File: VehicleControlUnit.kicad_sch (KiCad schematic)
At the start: 33 parts, among them J1 Conn_01x02, J10 CAR_CAN_Breakout, J2 Precharge_Ready, J4 Conn_01x02, J5 Conn_01x02, J6 Conn_01x08, J7 Conn_01x04, J8 Conn_01x04, J9 MOTOR_CAN_Breakout, Q1 PMV35EPER

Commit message: fuck the rats nest im doing it tomorrow
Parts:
- removed J10: CAR_CAN_Breakout, Connector_PinHeader_2.54mm:PinHeader_1x02_P2.54mm_Vertical, symbol Connector_Generic:Conn_01x02
- removed J2: Precharge_Ready, Connector_Molex:Molex_Nano-Fit_105309-xx02_1x02_P2.50mm_Vertical, symbol Connector_Generic:Conn_01x02
- removed J6: Conn_01x08, Connector_PinHeader_2.54mm:PinHeader_1x08_P2.54mm_Vertical, symbol Connector_Generic:Conn_01x08
- removed J9: MOTOR_CAN_Breakout, Connector_PinHeader_2.54mm:PinHeader_1x02_P2.54mm_Vertical, symbol Connector_Generic:Conn_01x02
- removed Q1: PMV35EPER, Package_TO_SOT_SMD:SOT-23-3, symbol Device:Q_PMOS
- removed R1: 49.9k, Resistor_SMD:R_0805_2012Metric, symbol Device:R_US
- removed R2: 100, Resistor_SMD:R_0805_2012Metric, symbol Device:R_US
- removed R3: 10k, Resistor_SMD:R_0805_2012Metric, symbol Device:R_US
- added C2: 22n, Capacitor_SMD:C_0805_2012Metric, symbol Device:C
- added J5, J6: SFH11-PBPC-D05-ST-BK, UTSVT_Connectors:CONN_SFH11-xxxC-D05-ST-XX_SUL, symbol UTSVT_Connectors:SFH11-PBPC-D05-ST-BK
- added Q1: PSMN8R5-40MSDX, UTSVT_Power:BUK7M1780EX, symbol UTSVT_Power:PSMN8R5-40MSDX
- added U1: LM74501-Q1, Package_TO_SOT_SMD:SOT-23-8, symbol UTSVT_ICs:LM74501-Q1
- C1: value 1u -> 220n
- D1: footprint Active-PrechargeLib:BZT52B12QX -> UTSVT_Passives:BZT52B12QX
- J1: footprint utsvt_conn:Molex_MicroFit3.0_1x2xP3.00mm_PolarizingPeg_Vertical -> UTSVT_Connectors:Molex_MicroFit3.0_1x2xP3.00mm_PolarizingPeg_Vertical
- J4: renamed from J3; footprint (none) -> UTSVT_Special:LeaderSOM
- renumbered C2 to C3, C3 to C4, J4 to J2, J5 to J3, R4 to R1, R5 to R2, R6 to R3, R7 to R4, R8 to R5
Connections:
- net +24V: now also Q1.10 (D_6), Q1.11 (D_7), Q1.5 (D_1), Q1.6 (D_2), Q1.7 (D_3), Q1.8 (D_4), Q1.9 (D_5), U1.8 (Drain)
- net C_CAN_H: now also J6.3
- net C_CAN_L: now also J6.4
- net ESP_RX: now also J6.5
- net ESP_TX: now also J6.6
- net GND: now also D1.2 (A), J5.10, J6.10, U1.5 (GND); no longer C1.2
- net LV+: now also C1.2, C2.2, Q1.1 (S_1), Q1.2 (S_2), Q1.3 (S_3), U1.2 (Source), U1.6 (EN)
- net MPre_Enable: now also J5.2
- net MPre_Sense: now also J5.4
- net M_CAN_H: now also J6.1
- net M_CAN_L: now also J6.2
- net M_Enable: now also J5.1
- net M_Sense: now also J5.3
- net Precharge_Ready: now also J5.8; no longer C1.1
- net VPrecharge+: now also J5.6
- net VPrecharge-: now also J5.7
- new net: C1.1, U1.3 (VCap)
- new net: C2.1, Q1.4 (G), U1.1 (Gate)
- no-connect marks 5 -> 12
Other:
- note added: "Precharge Board Connectors"
- note removed: "From Optocoupler on Precharge Board"
- note removed: "Lowpass Filter Fc = 1.6kHz"
- note removed: "Precharge Connectors"
- moved on the sheet: 24V_TP1, D1, J1, J2, J3, J7, J8, LVGND_TP1

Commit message: routing done
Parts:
- added C19: 0.1u, Capacitor_SMD:C_0805_2012Metric, symbol Device:C
- J2, J3: footprint Connector_Molex:Molex_Nano-Fit_105309-xx02_1x02_P2.50mm_Vertical -> UTSVT_Connectors:Molex_Nano-Fit_105309-xx02_1x02_P2.50mm_Vertical
- J7, J8: footprint Connector_Molex:Molex_Nano-Fit_105309-xx04_1x04_P2.50mm_Vertical -> UTSVT_Connectors:Molex_Nano-Fit_105309-xx04_1x04_P2.50mm_Vertical
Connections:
- net Precharge_Ready is gone; now on net MPre_Sense: J5.8
- net 3V3_LSOM: now also J5.1
- net ESP_RX: now also J6.6; no longer J6.5
- net ESP_TX: now also J6.5; no longer J6.6
- net GND: now also J5.9, J6.9, C19.2
- net LV+: now also C19.1
- net MPre_Enable: now also J5.3; no longer J5.2
- net MPre_Sense: no longer J5.4
- net M_Enable: now also J5.2; no longer J5.1
- net M_Sense: now also J5.7; no longer J5.3
- net VPrecharge-: now also J5.4; no longer J5.7
- no-connect marks 12 -> 10
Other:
- moved on the sheet: C3, C4, LVPWR1, R1

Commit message: replace microfit with nanofit and some layout adjustments
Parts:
- J1: footprint UTSVT_Connectors:Molex_MicroFit3.0_1x2xP3.00mm_PolarizingPeg_Vertical -> UTSVT_Connectors:Molex_Nano-Fit_105309-xx02_1x02_P2.50mm_Vertical
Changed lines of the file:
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@@
 			)
 		)
-		(property "Footprint" "UTSVT_Connectors:Molex_MicroFit3.0_1x2xP3.00mm_PolarizingPeg_Vertical"
+		(property "Footprint" "UTSVT_Connectors:Molex_Nano-Fit_105309-xx02_1x02_P2.50mm_Vertical"
 			(at 26.035 41.91 0)
 			(effects

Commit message: lakshay nitpicks
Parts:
- removed J6: SFH11-PBPC-D05-ST-BK, UTSVT_Connectors:CONN_SFH11-xxxC-D05-ST-XX_SUL, symbol UTSVT_Connectors:SFH11-PBPC-D05-ST-BK
- added J8: Conn_01x04, Connector_PinHeader_2.54mm:PinHeader_1x04_P2.54mm_Vertical, symbol Connector_Generic:Conn_01x04
- renumbered C19 to C5, J7 to J6, J8 to J7
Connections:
- net 3V3_LSOM: no longer J5.1
- net C_CAN_H: now also J6.4 (Pin_4), J8.4 (Pin_4); no longer J6.2 (Pin_2)
- net C_CAN_L: now also J6.3 (Pin_3), J8.3 (Pin_3); no longer J6.1 (Pin_1)
- net ESP_RX: now also J5.8
- net ESP_TX: now also J5.7
- net MPre_Enable: now also J5.2; no longer J5.3
- net MPre_Sense: now also J5.3; no longer J5.8
- net M_CAN_H: now also J6.2 (Pin_2), J8.2 (Pin_2); no longer J6.4 (Pin_4)
- net M_CAN_L: now also J6.1 (Pin_1), J8.1 (Pin_1); no longer J6.3 (Pin_3)
- net M_Enable: now also J5.4; no longer J5.2
- net M_Sense: now also J5.1; no longer J5.7
- net Motor_Voltage: now reaches J5.5
- net Motor_Voltage: now also J3.2 (Pin_2), J4.16 (SPI2_CS)
- net VPrecharge+ renamed Batt_Voltage
- removed net VPrecharge-: J3.2 (Pin_2), J4.16 (SPI2_CS), J5.4
- no-connect marks 10 -> 7

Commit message: cubemx stuff
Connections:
- net ESP_RX: now also J4.19 (UART5_RX), J5.7; no longer J4.17 (UART5_TX), J5.8
- net ESP_TX: now also J4.17 (UART5_TX), J5.8; no longer J4.19 (UART5_RX), J5.7
- net MPre_Enable: now also J4.16 (SPI2_CS); no longer J4.9 (I2C3_SDA)
- net Motor_Voltage: now also J4.9 (I2C3_SDA); no longer J4.16 (SPI2_CS)
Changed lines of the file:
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@@
+	(wire
+		(pts
+			(xy 44.45 109.22) (xy 31.75 109.22)
+		)
+		(stroke
+			(width 0)
+			(type default)
+		)
+	)
 	(wire
 		(pts
@@
 	(wire
 		(pts
-			(xy 77.47 101.6) (xy 95.25 101.6)
-		)
-		(stroke
-			(width 0)
-			(type default)
-		)
-	)
-	(wire
-		(pts
 			(xy 199.39 27.94) (xy 199.39 30.48)
 		)
@@
 	(wire
 		(pts
+			(xy 95.25 101.6) (xy 77.47 101.6)
+		)
+		(stroke
+			(width 0)
+			(type default)
+		)
+	)
+	(wire
+		(pts
 			(xy 76.835 32.385) (xy 76.835 34.925)
 		)
@@
 		(pts
 			(xy 243.84 125.73) (xy 248.92 125.73)
-		)
-		(stroke
-			(width 0)
-			(type default)
-		)
-	)
-	(wire
-		(pts
-			(xy 31.75 109.22) (xy 44.45 109.22)
 		)
 		(stroke
@@
 		)
 	)
-	(label "MPre_Enable"
-		(at 31.75 109.22 0)
-		(effects
-			(font
-				(size 1.27 1.27)
-			)
-			(justify left bottom)
-		)
-	)
 	(label "M_CAN_L"
 		(at 236.22 58.42 0)
@@
 		)
 	)
+	(label "ESP_RX"
+		(at 166.37 113.03 0)
+		(effects
+			(font
+				(size 1.27 1.27)
+			)
+			(justify left bottom)
+		)
+	)
 	(label "M_Sense"
 		(at 166.37 97.79 0)
@@
 	)
 	(label "ESP_RX"
-		(at 35.56 99.06 0)
+		(at 35.56 96.52 0)
 		(effects
 			(font
@@
 		)
 	)
+	(label "Motor_Voltage"
+		(at 31.75 109.22 0)
+		(effects
+			(font
+				(size 1.27 1.27)
+			)
+			(justify left bottom)
+		)
+	)
 	(label "LED1"
 		(at 165.1 27.94 0)
@@
 		)
 	)
+	(label "ESP_TX"
+		(at 166.37 115.57 0)
+		(effects
+			(font
+				(size 1.27 1.27)
+			)
+			(justify left bottom)
+		)
+	)
 	(label "C_CAN_L"
 		(at 236.22 33.655 0)
@@
 		)
 	)
-	(label "ESP_TX"
-		(at 35.56 96.52 0)
-		(effects
-			(font
-				(size 1.27 1.27)
-			)
-			(justify left bottom)
-		)
-	)
 	(label "C_CAN_H"
 		(at 236.22 36.195 0)
@@
 		)
 	)
-	(label "ESP_RX"
-		(at 166.37 115.57 0)
-		(effects
-			(font
-				(size 1.27 1.27)
-			)
-			(justify left bottom)
-		)
-	)
 	(label "LED4"
 		(at 199.39 27.94 0)
@@
 		)
 	)
-	(label "ESP_TX"
-		(at 166.37 113.03 0)
-		(effects
-			(font
-				(size 1.27 1.27)
-			)
-			(justify left bottom)
-		)
-	)
 	(label "C_CAN_L"
 		(at 162.56 111.76 180)
@@
 		)
 	)
+	(label "MPre_Enable"
+		(at 95.25 101.6 180)
+		(effects
+			(font
+				(size 1.27 1.27)
+			)
+			(justify right bottom)
+		)
+	)
 	(label "C_CAN_L"
 		(at 236.22 48.26 0)
@@
 		)
 	)
+	(label "ESP_TX"
+		(at 35.56 99.06 0)
+		(effects
+			(font
+				(size 1.27 1.27)
+			)
+			(justify left bottom)
+		)
+	)
 	(label "M_CAN_H"
 		(at 236.22 45.72 0)
@@
 		(effects
 			(font
-				(size 1.27 1.27)
-			)
-			(justify right bottom)
-		)
-	)
-	(label "Motor_Voltage"
-		(at 95.25 101.6 180)
-		(effects
-			(font

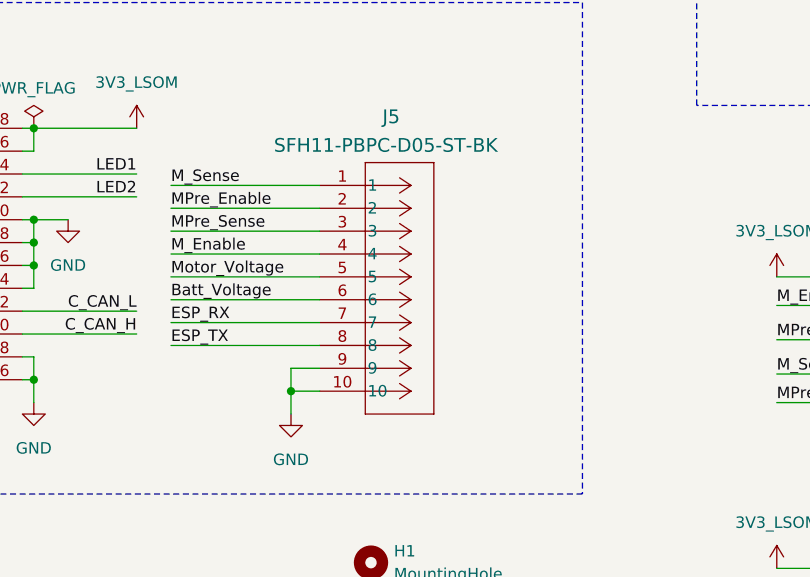
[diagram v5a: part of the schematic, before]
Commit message: replaced 0805 with 0603, changed logic analyzer symbol and silkscreen
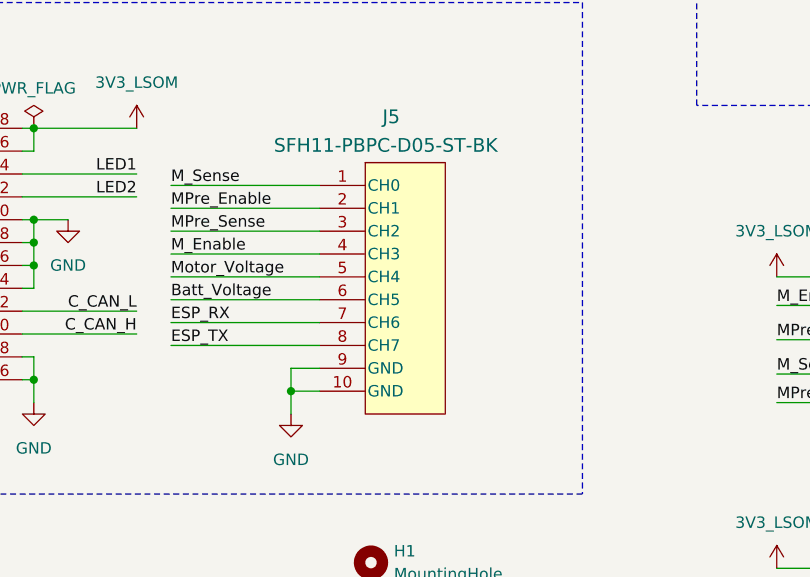
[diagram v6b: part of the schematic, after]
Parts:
- C1, C2, C3, C4, C5: footprint Capacitor_SMD:C_0805_2012Metric -> Capacitor_SMD:C_0603_1608Metric
- LED1, LED2, LED3, LED4, LVPWR1: footprint LED_SMD:LED_0805_2012Metric -> LED_SMD:LED_0603_1608Metric
- R1, R2, R3, R4, R5: footprint Resistor_SMD:R_0805_2012Metric -> Resistor_SMD:R_0603_1608Metric
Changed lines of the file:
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@@
 			)
 		)
-		(property "Footprint" "Capacitor_SMD:C_0805_2012Metric"
+		(property "Footprint" "Capacitor_SMD:C_0603_1608Metric"
 			(at 46.0502 52.705 0)
 			(effects
@@
 			)
 		)
-		(property "Footprint" "LED_SMD:LED_0805_2012Metric"
+		(property "Footprint" "LED_SMD:LED_0603_1608Metric"
 			(at 187.96 43.18 0)
 			(effects
@@
 			)
 		)
-		(property "Footprint" "Resistor_SMD:R_0805_2012Metric"
+		(property "Footprint" "Resistor_SMD:R_0603_1608Metric"
 			(at 166.116 34.544 90)
 			(effects
@@
 			)
 		)
-		(property "Footprint" "Capacitor_SMD:C_0805_2012Metric"
+		(property "Footprint" "Capacitor_SMD:C_0603_1608Metric"
 			(at 141.3002 41.91 0)
 			(effects
@@
 			)
 		)
-		(property "Footprint" "Resistor_SMD:R_0805_2012Metric"
+		(property "Footprint" "Resistor_SMD:R_0603_1608Metric"
 			(at 188.976 34.544 90)
 			(effects
@@
 			)
 		)
-		(property "Footprint" "LED_SMD:LED_0805_2012Metric"
+		(property "Footprint" "LED_SMD:LED_0603_1608Metric"
 			(at 199.39 43.18 0)
 			(effects
@@
 			)
 		)
-		(property "Footprint" "Capacitor_SMD:C_0805_2012Metric"
+		(property "Footprint" "Capacitor_SMD:C_0603_1608Metric"
 			(at 49.8602 34.29 0)
 			(effects
@@
 			)
 		)
-		(property "Footprint" "Resistor_SMD:R_0805_2012Metric"
+		(property "Footprint" "Resistor_SMD:R_0603_1608Metric"
 			(at 200.406 34.544 90)
 			(effects
@@
 			)
 		)
-		(property "Footprint" "Resistor_SMD:R_0805_2012Metric"
+		(property "Footprint" "Resistor_SMD:R_0603_1608Metric"
 			(at 177.546 34.544 90)
 			(effects
@@
 			)
 		)
-		(property "Footprint" "Capacitor_SMD:C_0805_2012Metric"
+		(property "Footprint" "Capacitor_SMD:C_0603_1608Metric"
 			(at 131.1402 41.91 0)
 			(effects
@@
 			)
 		)
-		(property "Footprint" "Resistor_SMD:R_0805_2012Metric"
+		(property "Footprint" "Resistor_SMD:R_0603_1608Metric"
 			(at 105.156 33.274 90)
 			(effects
@@
 			)
 		)
-		(property "Footprint" "LED_SMD:LED_0805_2012Metric"
+		(property "Footprint" "LED_SMD:LED_0603_1608Metric"
 			(at 165.1 43.18 0)
 			(effects
@@
 			)
 		)
-		(property "Footprint" "Capacitor_SMD:C_0805_2012Metric"
+		(property "Footprint" "Capacitor_SMD:C_0603_1608Metric"
 			(at 118.4402 41.91 0)
 			(effects
@@
 			)
 		)
-		(property "Footprint" "LED_SMD:LED_0805_2012Metric"
+		(property "Footprint" "LED_SMD:LED_0603_1608Metric"
 			(at 176.53 43.18 0)
 			(effects
@@
 			)
 		)
-		(property "Footprint" "LED_SMD:LED_0805_2012Metric"
+		(property "Footprint" "LED_SMD:LED_0603_1608Metric"
 			(at 104.14 41.91 0)
 			(effects

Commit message: embedding 3d models
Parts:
- U1: footprint Package_TO_SOT_SMD:SOT-23-8 -> UTSVT_ICs:LM74501QDDFRQ1
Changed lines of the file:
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@@
 			)
 		)
-		(property "Footprint" "Package_TO_SOT_SMD:SOT-23-8"
+		(property "Footprint" "UTSVT_ICs:LM74501QDDFRQ1"
 			(at 64.135 48.26 0)
 			(effects

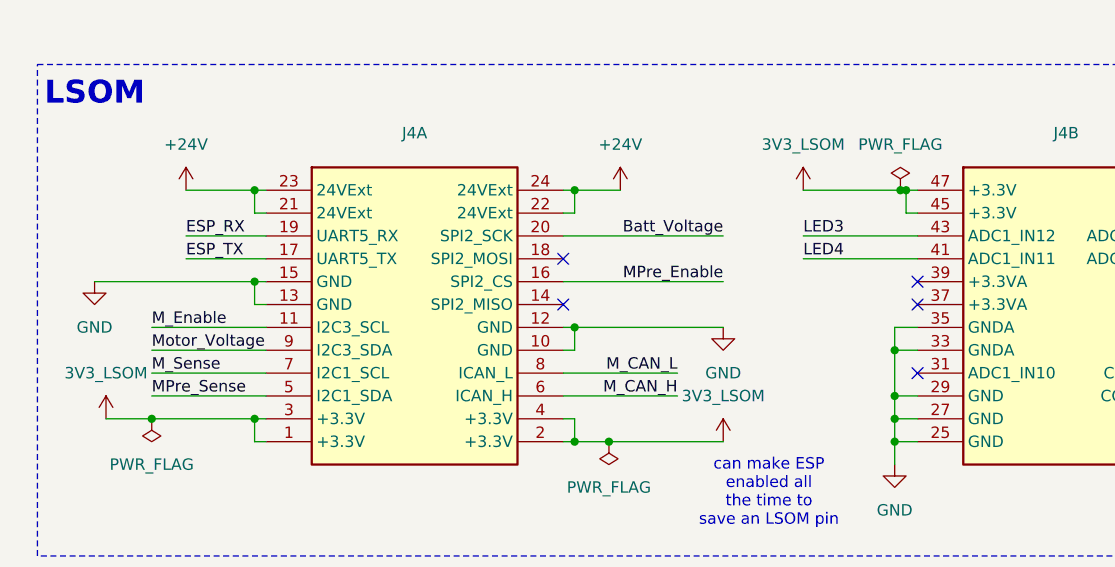
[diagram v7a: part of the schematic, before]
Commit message: added image to schematic
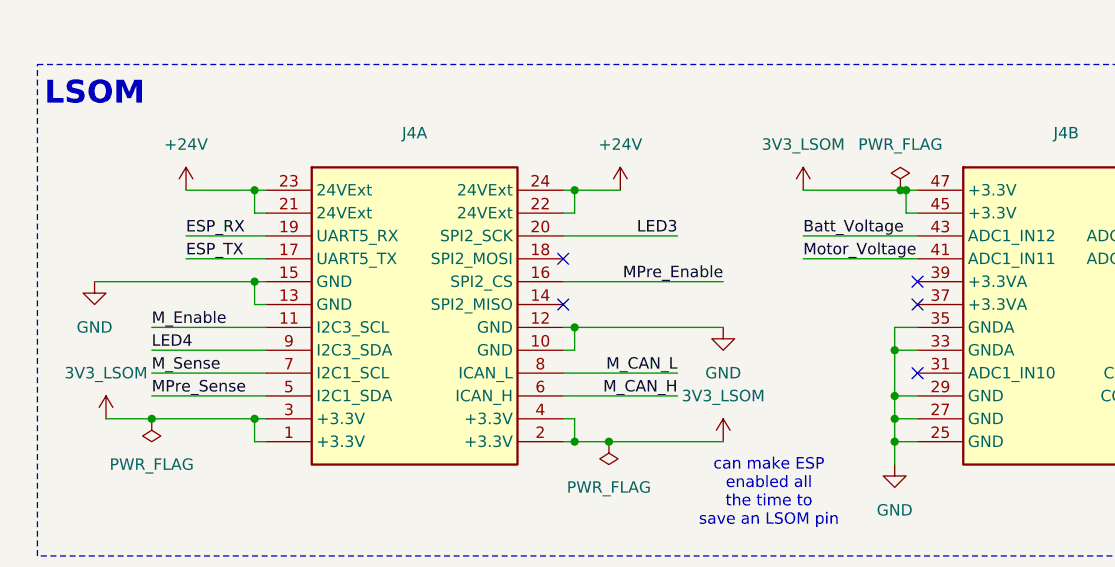
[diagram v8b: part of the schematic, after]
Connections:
- net Batt_Voltage: now also J4.43 (ADC1_IN12); no longer J4.20 (SPI2_SCK)
- net LED3: now also J4.20 (SPI2_SCK); no longer J4.43 (ADC1_IN12)
- net LED4: now also J4.9 (I2C3_SDA); no longer J4.41 (ADC1_IN11)
- net Motor_Voltage: now also J4.41 (ADC1_IN11); no longer J4.9 (I2C3_SDA)
